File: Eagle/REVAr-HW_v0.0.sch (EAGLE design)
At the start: 97 parts, among them IC1 MC33269ST-5.0T3, IC2 MC33269D-5.0, IC3 ATMEGA2560-16AU, IC4 ATMEGA8U2-MU, IC5 LM358D, IC6 LP2985-33DBVR, IC7 PCF8574T, Q1 16MHz, Q2 16MHz, T2 FDN340P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

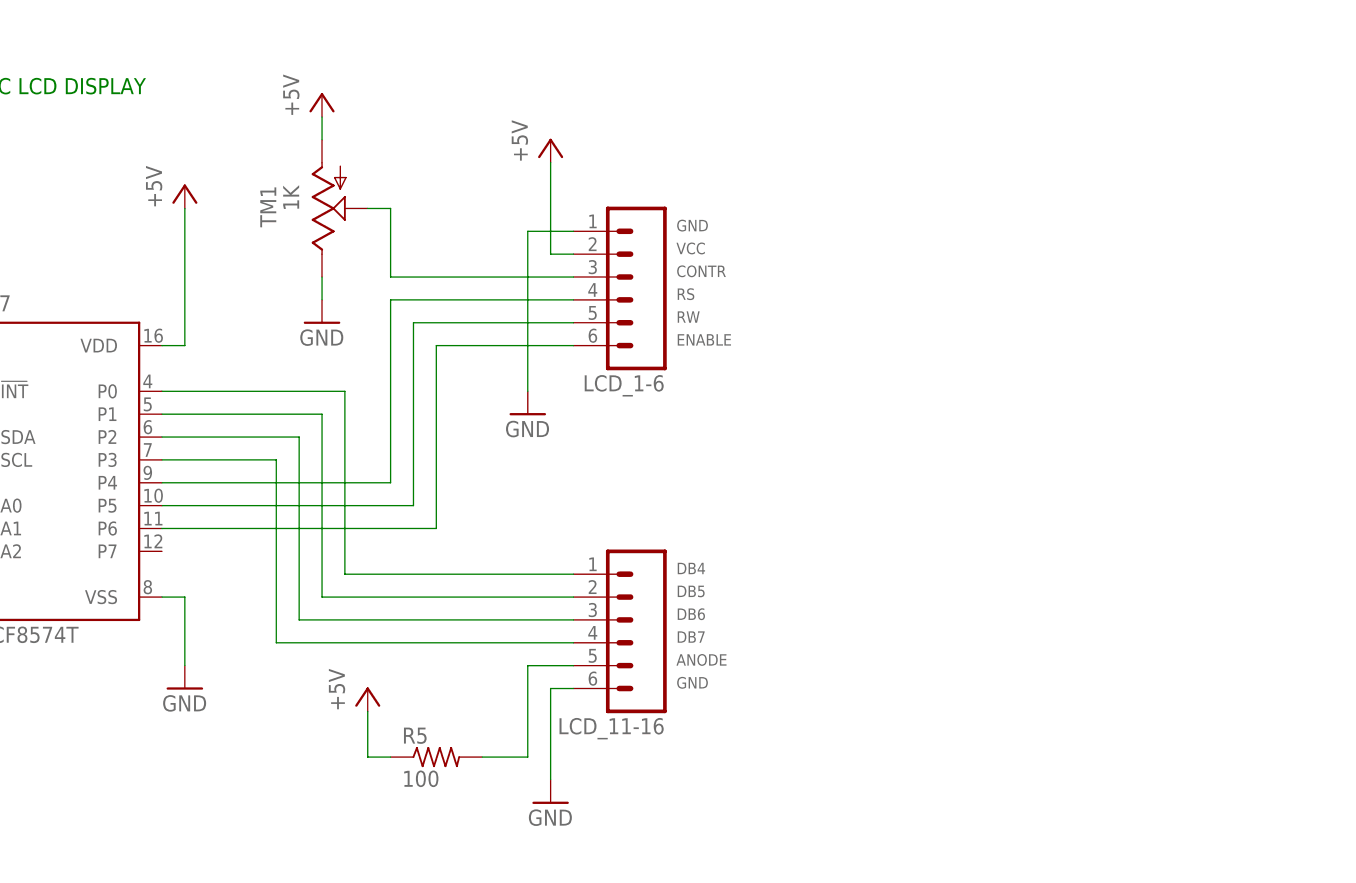
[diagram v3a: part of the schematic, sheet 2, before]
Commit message: [HW] Add push buttons for user interface
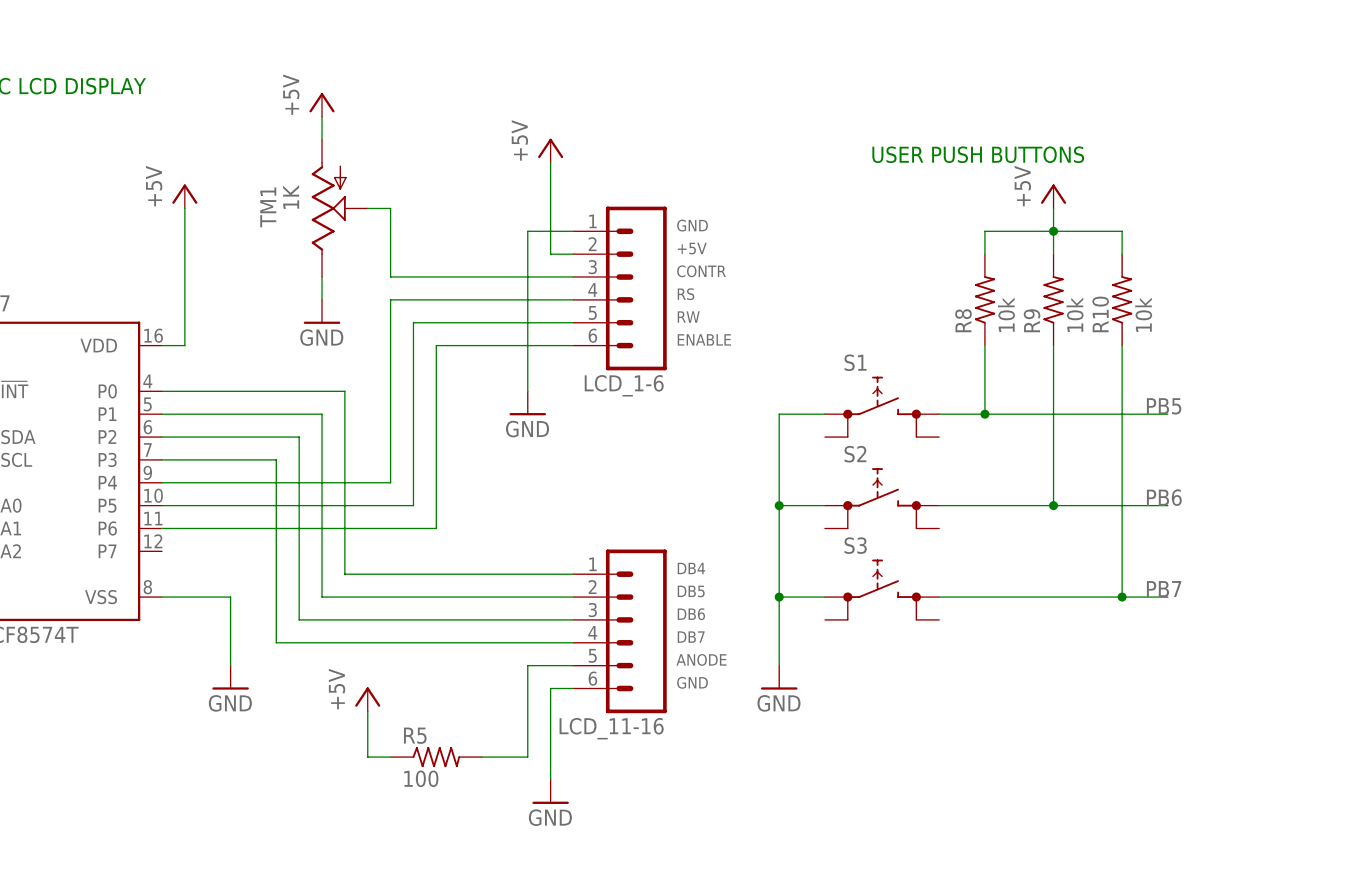
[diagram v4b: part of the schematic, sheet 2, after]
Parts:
- added R10, R8, R9: 10k, adafruit:R-US_R0805
- added S1, S2, S3: (no value), switch:REKN
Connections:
- net +5V: now also LCD_1-6.2
- net GND: now also S1.0@A, S2.0@A, S3.0@A
- net PB5: now also R8.1, S1.1@A
- net PB6: now also R9.1, S2.1@A
- net PB7: now also R10.1, S3.1@A
- net VCC: now also R10.2, R8.2, R9.2; no longer LCD_1-6.2
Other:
- note added: "USER PUSH BUTTONS"
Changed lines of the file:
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@@
 <layer number="54" name="bGND_GNDA" color="7" fill="1" visible="no" active="no"/>
 <layer number="56" name="wert" color="7" fill="1" visible="no" active="no"/>
+<layer number="57" name="tCAD" color="7" fill="1" visible="no" active="no"/>
 <layer number="88" name="SimResults" color="9" fill="1" visible="yes" active="yes"/>
 <layer number="89" name="SimProbes" color="9" fill="1" visible="yes" active="yes"/>
@@
 <layer number="97" name="Info" color="7" fill="1" visible="no" active="yes"/>
 <layer number="98" name="Guide" color="6" fill="1" visible="no" active="yes"/>
+<layer number="99" name="SpiceOrder" color="7" fill="1" visible="no" active="no"/>
 <layer number="100" name="Muster" color="7" fill="1" visible="no" active="no"/>
 <layer number="101" name="Hidden" color="15" fill="1" visible="yes" active="yes"/>
@@
 <layer number="111" name="LPC17xx" color="7" fill="1" visible="yes" active="yes"/>
 <layer number="112" name="tSilk" color="7" fill="1" visible="yes" active="yes"/>
+<layer number="113" name="ReferenceLS" color="7" fill="1" visible="no" active="no"/>
 <layer number="116" name="Patch_BOT" color="9" fill="4" visible="no" active="yes"/>
+<layer number="118" name="Rect_Pads" color="7" fill="1" visible="no" active="no"/>
 <layer number="121" name="_tsilk" color="7" fill="1" visible="no" active="yes"/>
 <layer number="122" name="_bsilk" color="7" fill="1" visible="no" active="yes"/>
@@
 <layer number="132" name="bAdjust" color="7" fill="1" visible="no" active="yes"/>
 <layer number="144" name="Drill_legend" color="7" fill="1" visible="no" active="yes"/>
+<layer number="150" name="Notes" color="7" fill="1" visible="no" active="yes"/>
 <layer number="151" name="HeatSink" color="7" fill="1" visible="no" active="yes"/>
 <layer number="152" name="_bDocu" color="7" fill="1" visible="yes" active="yes"/>
+<layer number="153" name="FabDoc1" color="6" fill="1" visible="no" active="no"/>
+<layer number="154" name="FabDoc2" color="2" fill="1" visible="no" active="no"/>
+<layer number="155" name="FabDoc3" color="7" fill="15" visible="no" active="no"/>
 <layer number="199" name="Contour" color="7" fill="1" visible="no" active="yes"/>
 <layer number="200" name="200bmp" color="1" fill="10" visible="no" active="yes"/>
@@
 <layer number="223" name="223bmp" color="24" fill="1" visible="no" active="no"/>
 <layer number="224" name="224bmp" color="25" fill="1" visible="no" active="no"/>
+<layer number="231" name="Eagle3D_PG1" color="7" fill="1" visible="no" active="no"/>
+<layer number="232" name="Eagle3D_PG2" color="7" fill="1" visible="no" active="no"/>
+<layer number="233" name="Eagle3D_PG3" color="7" fill="1" visible="no" active="no"/>
 <layer number="248" name="Housing" color="7" fill="1" visible="yes" active="yes"/>
 <layer number="249" name="Edge" color="7" fill="1" visible="yes" active="yes"/>
@@
 <part name="P+35" library="supply1" library_urn="urn:adsk.eagle:library:371" deviceset="VCC" device="" value="+5V"/>
 <part name="P+36" library="supply1" library_urn="urn:adsk.eagle:library:371" deviceset="VCC" device="" value="+5V"/>
+<part name="S1" library="switch" deviceset="REKN" device=""/>
+<part name="S2" library="switch" deviceset="REKN" device=""/>
+<part name="S3" library="switch" deviceset="REKN" device=""/>
+<part name="GND46" library="SparkFun-Aesthetics" deviceset="GND" device=""/>
+<part name="P+37" library="supply1" library_urn="urn:adsk.eagle:library:371" deviceset="VCC" device="" value="+5V"/>
+<part name="R8" library="adafruit" deviceset="R-US_" device="R0805" value="10k"/>
+<part name="R9" library="adafruit" deviceset="R-US_" device="R0805" value="10k"/>
+<part name="R10" library="adafruit" deviceset="R-US_" device="R0805" value="10k"/>
 </parts>
 <sheets>
@@
 <text x="279.4" y="132.08" size="1.778" layer="91">TO ARDUINO</text>
 <text x="71.12" y="292.1" size="1.778" layer="91">I2C LCD DISPLAY</text>
+<text x="170.18" y="284.48" size="1.778" layer="91">USER PUSH BUTTONS</text>
 </plain>
 <instances>
@@
 <instance part="GND47" gate="1" x="132.08" y="256.54"/>
 <instance part="GND48" gate="1" x="109.22" y="266.7"/>
-<instance part="GND49" gate="1" x="93.98" y="226.06"/>
+<instance part="GND49" gate="1" x="99.06" y="226.06"/>
 <instance part="GND50" gate="1" x="134.62" y="213.36"/>
 <instance part="R7" gate="G$1" x="48.26" y="284.48" rot="R90"/>
@@
 <instance part="P+35" gate="VCC" x="114.3" y="226.06"/>
 <instance part="P+36" gate="VCC" x="35.56" y="248.92"/>
+<instance part="S1" gate="G$1" x="170.18" y="256.54"/>
+<instance part="S2" gate="G$1" x="170.18" y="246.38"/>
+<instance part="S3" gate="G$1" x="170.18" y="236.22"/>
+<instance part="GND46" gate="1" x="160.02" y="226.06"/>
+<instance part="P+37" gate="VCC" x="190.5" y="281.94"/>
+<instance part="R8" gate="G$1" x="182.88" y="269.24" rot="R90"/>
+<instance part="R9" gate="G$1" x="190.5" y="269.24" rot="R90"/>
+<instance part="R10" gate="G$1" x="198.12" y="269.24" rot="R90"/>
 </instances>
 <busses>
@@
 </segment>
 <segment>
-<pinref part="IC7" gate="G$1" pin="VSS"/>
-<wire x1="91.44" y1="236.22" x2="93.98" y2="236.22" width="0.1524" layer="91"/>
-<pinref part="GND49" gate="1" pin="GND"/>
-<wire x1="93.98" y1="236.22" x2="93.98" y2="228.6" width="0.1524" layer="91"/>
-</segment>
-<segment>
 <pinref part="LCD_11-16" gate="G$1" pin="6"/>
 <wire x1="137.16" y1="226.06" x2="134.62" y2="226.06" width="0.1524" layer="91"/>
@@
 <junction x="50.8" y="213.36"/>
 </segment>
+<segment>
+<pinref part="GND49" gate="1" pin="GND"/>
+<wire x1="99.06" y1="228.6" x2="99.06" y2="236.22" width="0.1524" layer="91"/>
+<pinref part="IC7" gate="G$1" pin="VSS"/>
+<wire x1="99.06" y1="236.22" x2="91.44" y2="236.22" width="0.1524" layer="91"/>
+</segment>
+<segment>
+<pinref part="S1" gate="G$1" pin="0@A"/>
+<wire x1="165.1" y1="256.54" x2="160.02" y2="256.54" width="0.1524" layer="91"/>
+<pinref part="GND46" gate="1" pin="GND"/>
+<wire x1="160.02" y1="256.54" x2="160.02" y2="246.38" width="0.1524" layer="91"/>
+<pinref part="S2" gate="G$1" pin="0@A"/>
+<wire x1="160.02" y1="246.38" x2="160.02" y2="236.22" width="0.1524" layer="91"/>
+<wire x1="160.02" y1="236.22" x2="160.02" y2="228.6" width="0.1524" layer="91"/>
+<wire x1="165.1" y1="246.38" x2="160.02" y2="246.38" width="0.1524" layer="91"/>
+<junction x="160.02" y="246.38"/>
+<pinref part="S3" gate="G$1" pin="0@A"/>
+<wire x1="165.1" y1="236.22" x2="160.02" y2="236.22" width="0.1524" layer="91"/>
+<junction x="160.02" y="236.22"/>
+</segment>
 </net>
 <net name="ESP-CS" class="0">
@@
 </segment>
 <segment>
-<pinref part="LCD_1-6" gate="G$1" pin="2"/>
-<wire x1="137.16" y1="274.32" x2="134.62" y2="274.32" width="0.1524" layer="91"/>
-<wire x1="134.62" y1="274.32" x2="134.62" y2="284.48" width="0.1524" layer="91"/>
-<label x="148.59" y="274.32" size="1.27" layer="95"/>
-<pinref part="P+34" gate="VCC" pin="VCC"/>
-</segment>
-<segment>
 <pinref part="R5" gate="G$1" pin="1"/>
 <wire x1="114.3" y1="223.52" x2="114.3" y2="218.44" width="0.1524" layer="91"/>
@@
 <pinref part="P+36" gate="VCC" pin="VCC"/>
 </segment>
+<segment>
+<pinref part="P+37" gate="VCC" pin="VCC"/>
+<pinref part="R9" gate="G$1" pin="2"/>
+<wire x1="190.5" y1="279.4" x2="190.5" y2="276.86" width="0.1524" layer="91"/>
+<pinref part="R8" gate="G$1" pin="2"/>
+<wire x1="190.5" y1="276.86" x2="190.5" y2="274.32" width="0.1524" layer="91"/>
+<wire x1="182.88" y1="274.32" x2="182.88" y2="276.86" width="0.1524" layer="91"/>
+<wire x1="182.88" y1="276.86" x2="190.5" y2="276.86" width="0.1524" layer="91"/>
+<junction x="190.5" y="276.86"/>
+<pinref part="R10" gate="G$1" pin="2"/>
+<wire x1="198.12" y1="274.32" x2="198.12" y2="276.86" width="0.1524" layer="91"/>
+<wire x1="198.12" y1="276.86" x2="190.5" y2="276.86" width="0.1524" layer="91"/>
+</segment>
 </net>
 <net name="ESP-RST" class="0">
@@
 </segment>
 </net>
+<net name="+5V" class="0">
+<segment>
+<pinref part="LCD_1-6" gate="G$1" pin="2"/>
+<wire x1="137.16" y1="274.32" x2="134.62" y2="274.32" width="0.1524" layer="91"/>
+<wire x1="134.62" y1="274.32" x2="134.62" y2="284.48" width="0.1524" layer="91"/>
+<label x="148.59" y="274.32" size="1.27" layer="95"/>
+<pinref part="P+34" gate="VCC" pin="VCC"/>
+</segment>
+</net>
+<net name="PB5" class="0">
+<segment>
+<pinref part="R8" gate="G$1" pin="1"/>
+<wire x1="182.88" y1="264.16" x2="182.88" y2="256.54" width="0.1524" layer="91"/>
+<pinref part="S1" gate="G$1" pin="1@A"/>
+<wire x1="182.88" y1="256.54" x2="177.8" y2="256.54" width="0.1524" layer="91"/>
+<wire x1="182.88" y1="256.54" x2="203.2" y2="256.54" width="0.1524" layer="91"/>
+<junction x="182.88" y="256.54"/>
+<label x="200.66" y="256.54" size="1.778" layer="95"/>
+</segment>
+</net>
+<net name="PB6" class="0">
+<segment>
+<pinref part="S2" gate="G$1" pin="1@A"/>
+<wire x1="190.5" y1="246.38" x2="177.8" y2="246.38" width="0.1524" layer="91"/>
+<pinref part="R9" gate="G$1" pin="1"/>
+<wire x1="190.5" y1="264.16" x2="190.5" y2="246.38" width="0.1524" layer="91"/>
+<wire x1="190.5" y1="246.38" x2="203.2" y2="246.38" width="0.1524" layer="91"/>
+<junction x="190.5" y="246.38"/>
+<label x="200.66" y="246.38" size="1.778" layer="95"/>
+</segment>
+</net>
+<net name="PB7" class="0">
+<segment>
+<pinref part="S3" gate="G$1" pin="1@A"/>
+<wire x1="198.12" y1="236.22" x2="177.8" y2="236.22" width="0.1524" layer="91"/>
+<pinref part="R10" gate="G$1" pin="1"/>
+<wire x1="198.12" y1="264.16" x2="198.12" y2="236.22" width="0.1524" layer="91"/>
+<wire x1="198.12" y1="236.22" x2="203.2" y2="236.22" width="0.1524" layer="91"/>
+<junction x="198.12" y="236.22"/>
+<label x="200.66" y="236.22" size="1.778" layer="95"/>
+</segment>
+</net>

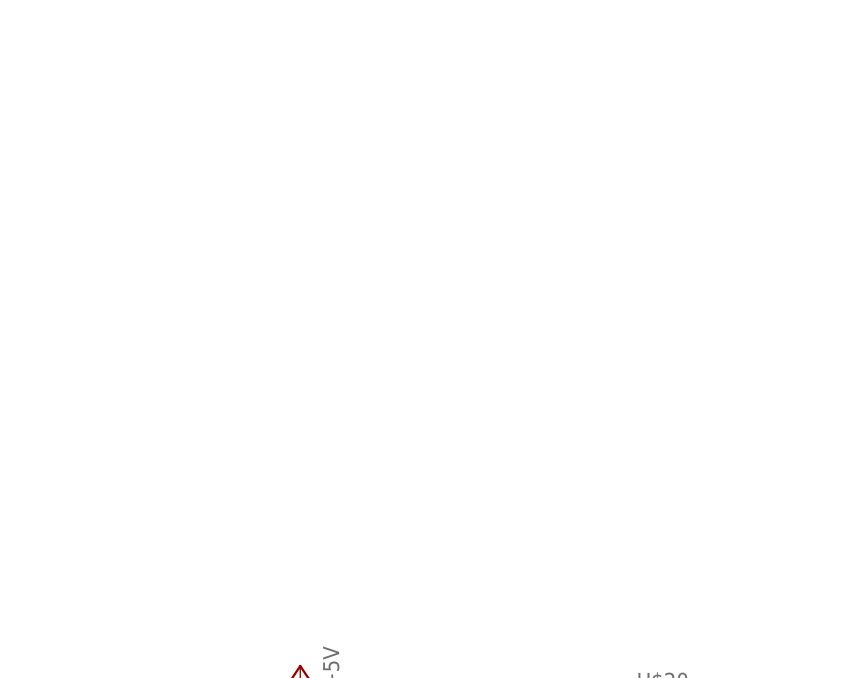
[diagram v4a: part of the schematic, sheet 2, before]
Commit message: [HW] Add SD Card Adapter
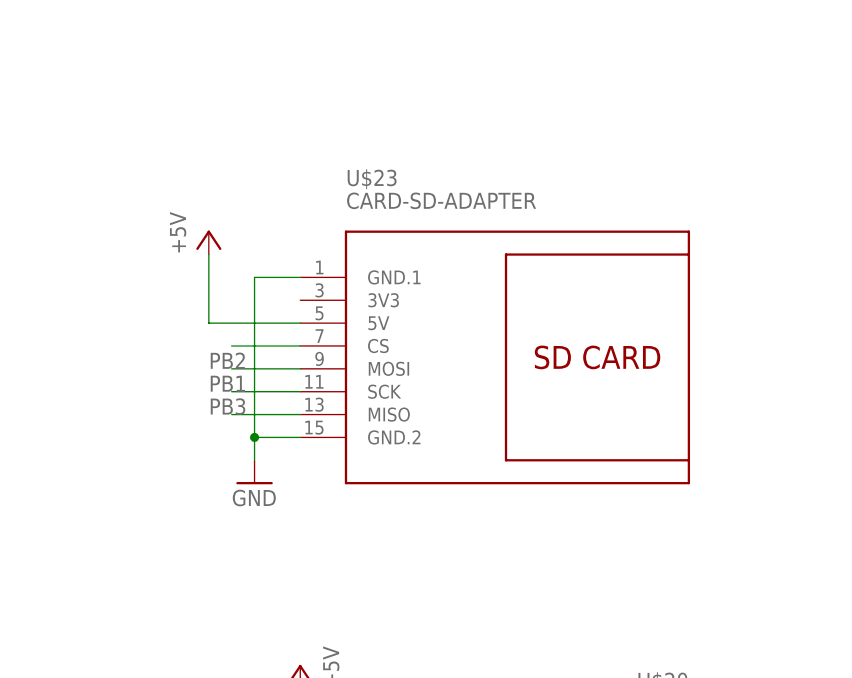
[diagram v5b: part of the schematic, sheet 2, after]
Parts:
- added U$23: CARD-SD-ADAPTER, diy-modules:CARD-SD-ADAPTER
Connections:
- new net N$18: U$23.CS
- net GND: now also U$23.GND.1, U$23.GND.2
- net PB1: now also U$23.SCK
- net PB2: now also U$23.MOSI
- net PB3: now also U$23.MISO
- net VCC: now also U$23.5V
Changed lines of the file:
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@@
 <part name="R9" library="adafruit" deviceset="R-US_" device="R0805" value="10k"/>
 <part name="R10" library="adafruit" deviceset="R-US_" device="R0805" value="10k"/>
+<part name="U$23" library="diy-modules" deviceset="CARD-SD-ADAPTER" device=""/>
+<part name="GND51" library="SparkFun-Aesthetics" deviceset="GND" device=""/>
+<part name="P+38" library="supply1" library_urn="urn:adsk.eagle:library:371" deviceset="VCC" device="" value="+5V"/>
 </parts>
 <sheets>
@@
 <instance part="R9" gate="G$1" x="190.5" y="269.24" rot="R90"/>
 <instance part="R10" gate="G$1" x="198.12" y="269.24" rot="R90"/>
+<instance part="U$23" gate="G$1" x="241.3" y="172.72"/>
+<instance part="GND51" gate="1" x="213.36" y="160.02"/>
+<instance part="P+38" gate="VCC" x="208.28" y="187.96"/>
 </instances>
 <busses>
@@
 <junction x="160.02" y="236.22"/>
 </segment>
+<segment>
+<pinref part="U$23" gate="G$1" pin="GND.1"/>
+<pinref part="GND51" gate="1" pin="GND"/>
+<wire x1="218.44" y1="182.88" x2="213.36" y2="182.88" width="0.1524" layer="91"/>
+<wire x1="213.36" y1="182.88" x2="213.36" y2="165.1" width="0.1524" layer="91"/>
+<pinref part="U$23" gate="G$1" pin="GND.2"/>
+<wire x1="213.36" y1="165.1" x2="213.36" y2="162.56" width="0.1524" layer="91"/>
+<wire x1="218.44" y1="165.1" x2="213.36" y2="165.1" width="0.1524" layer="91"/>
+<junction x="213.36" y="165.1"/>
+</segment>
 </net>
 <net name="ESP-CS" class="0">
@@
 <wire x1="198.12" y1="276.86" x2="190.5" y2="276.86" width="0.1524" layer="91"/>
 </segment>
+<segment>
+<pinref part="P+38" gate="VCC" pin="VCC"/>
+<wire x1="208.28" y1="185.42" x2="208.28" y2="177.8" width="0.1524" layer="91"/>
+<pinref part="U$23" gate="G$1" pin="5V"/>
+<wire x1="208.28" y1="177.8" x2="218.44" y2="177.8" width="0.1524" layer="91"/>
+</segment>
 </net>
 <net name="ESP-RST" class="0">
@@
 </segment>
 </net>
+<net name="PB2" class="0">
+<segment>
+<pinref part="U$23" gate="G$1" pin="MOSI"/>
+<wire x1="218.44" y1="172.72" x2="210.82" y2="172.72" width="0.1524" layer="91"/>
+<label x="208.28" y="172.72" size="1.778" layer="95"/>
+</segment>
+</net>
+<net name="PB1" class="0">
+<segment>
+<pinref part="U$23" gate="G$1" pin="SCK"/>
+<wire x1="218.44" y1="170.18" x2="210.82" y2="170.18" width="0.1524" layer="91"/>
+<label x="208.28" y="170.18" size="1.778" layer="95"/>
+</segment>
+</net>
+<net name="N$18" class="0">
+<segment>
+<pinref part="U$23" gate="G$1" pin="CS"/>
+<wire x1="218.44" y1="175.26" x2="210.82" y2="175.26" width="0.1524" layer="91"/>
+</segment>
+</net>
+<net name="PB3" class="0">
+<segment>
+<pinref part="U$23" gate="G$1" pin="MISO"/>
+<wire x1="218.44" y1="167.64" x2="210.82" y2="167.64" width="0.1524" layer="91"/>
+<label x="208.28" y="167.64" size="1.778" layer="95"/>
+</segment>
+</net>
